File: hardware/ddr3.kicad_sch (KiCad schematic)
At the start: 8 parts, among them U2 H5TQ4G63EFR

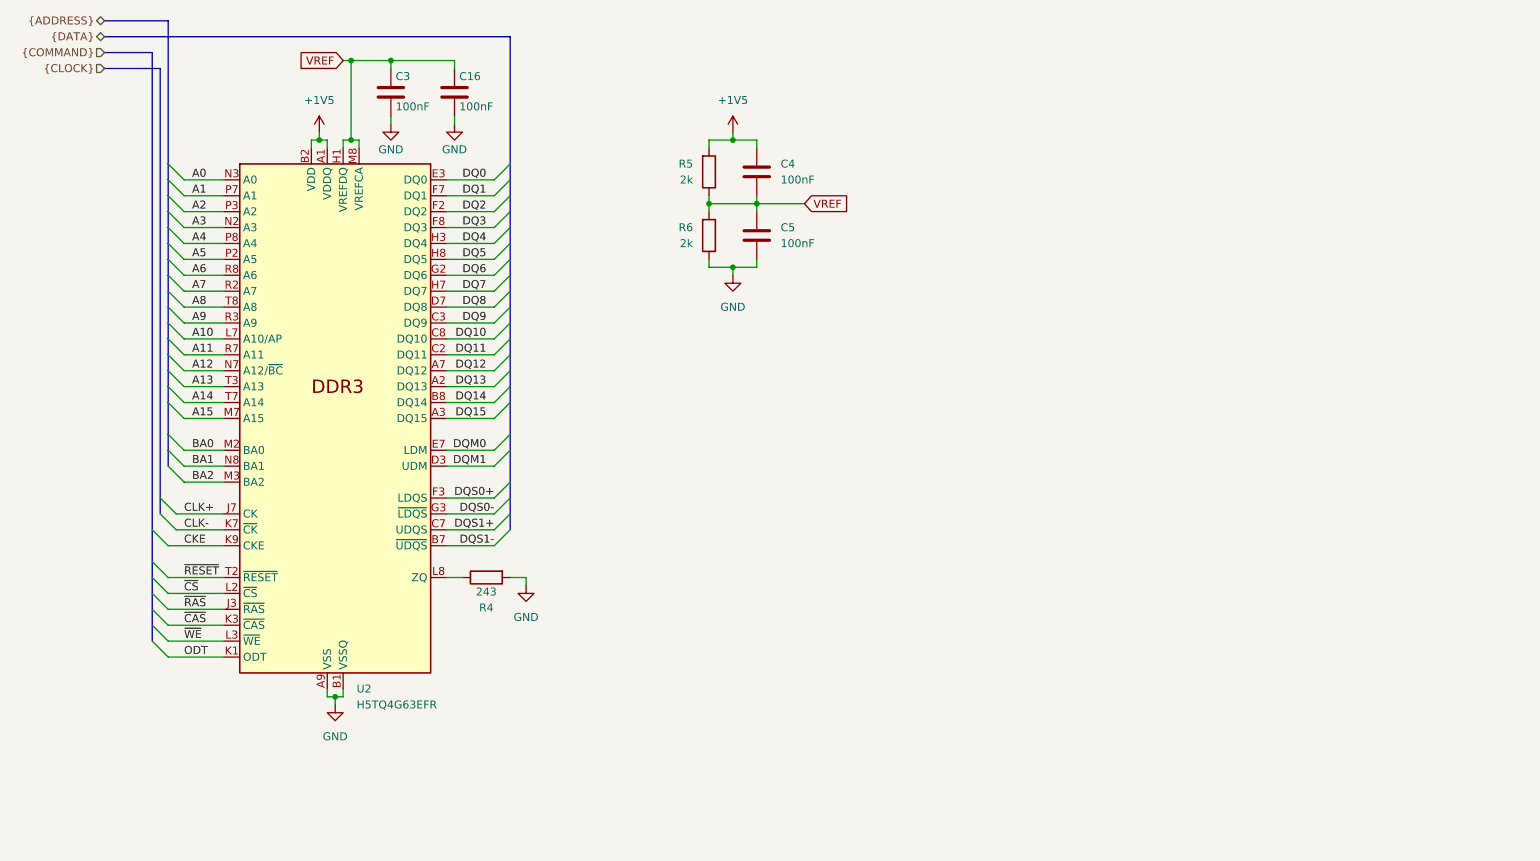
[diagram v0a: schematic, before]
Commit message: Decoupled DDR3 and drew RJ45 connector
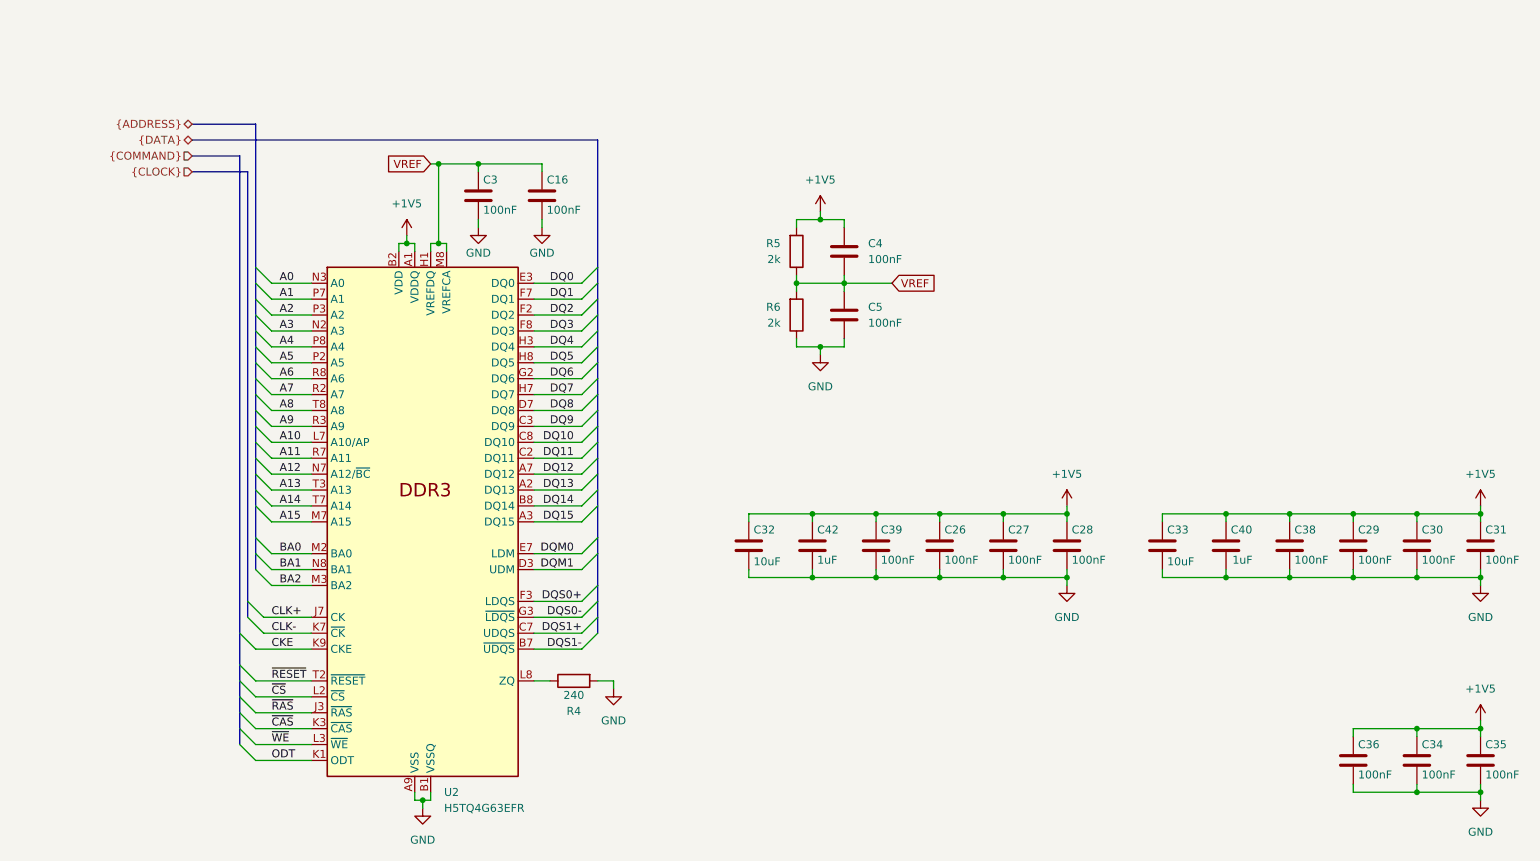
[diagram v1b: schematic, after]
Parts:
- added C26, C27, C28, C29, C30, C31, C34, C35, C36, C38, C39: 100nF, Capacitor_SMD:C_0402_1005Metric, symbol Device:C
- added C32, C33: 10uF, Capacitor_SMD:C_0603_1608Metric, symbol Device:C
- added C40, C42: 1uF, Capacitor_SMD:C_0402_1005Metric, symbol Device:C
- C16, C3, C4, C5: LCSC Part # (none) -> C1525
- R4: value 243 -> 240; LCSC Part # (none) -> C23350
- R5, R6: footprint Resistor_SMD:R_0603_1608Metric -> Resistor_SMD:R_0402_1005Metric; LCSC Part # (none) -> C4109
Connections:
- net +1V5: now also C26.1, C27.1, C28.1, C29.1, C30.1, C31.1, C32.1, C33.1, C34.1, C35.1, C36.1, C38.1, C39.1, C40.2, C42.2
- net GND: now also C26.2, C27.2, C28.2, C29.2, C30.2, C31.2, C32.2, C33.2, C34.2, C35.2, C36.2, C38.2, C39.2, C40.1, C42.1
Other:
- company: (none) -> Icy Electronics
- title: (none) -> Icepi CM0
- moved on the sheet: C16, C3, C4, C5, R4, R5, R6, U2

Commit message: Initial layout
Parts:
- renumbered C5 to C10, C39 to C11, C26 to C12, C27 to C13, C28 to C14, C33 to C15, C40 to C16, C38 to C17, C29 to C18, C36 to C19, C30 to C20, C34 to C21, C31 to C22, C35 to C23, C3 to C5, C16 to C6, C32 to C7, C42 to C8, C4 to C9, R4 to R5, R5 to R6, R6 to R7

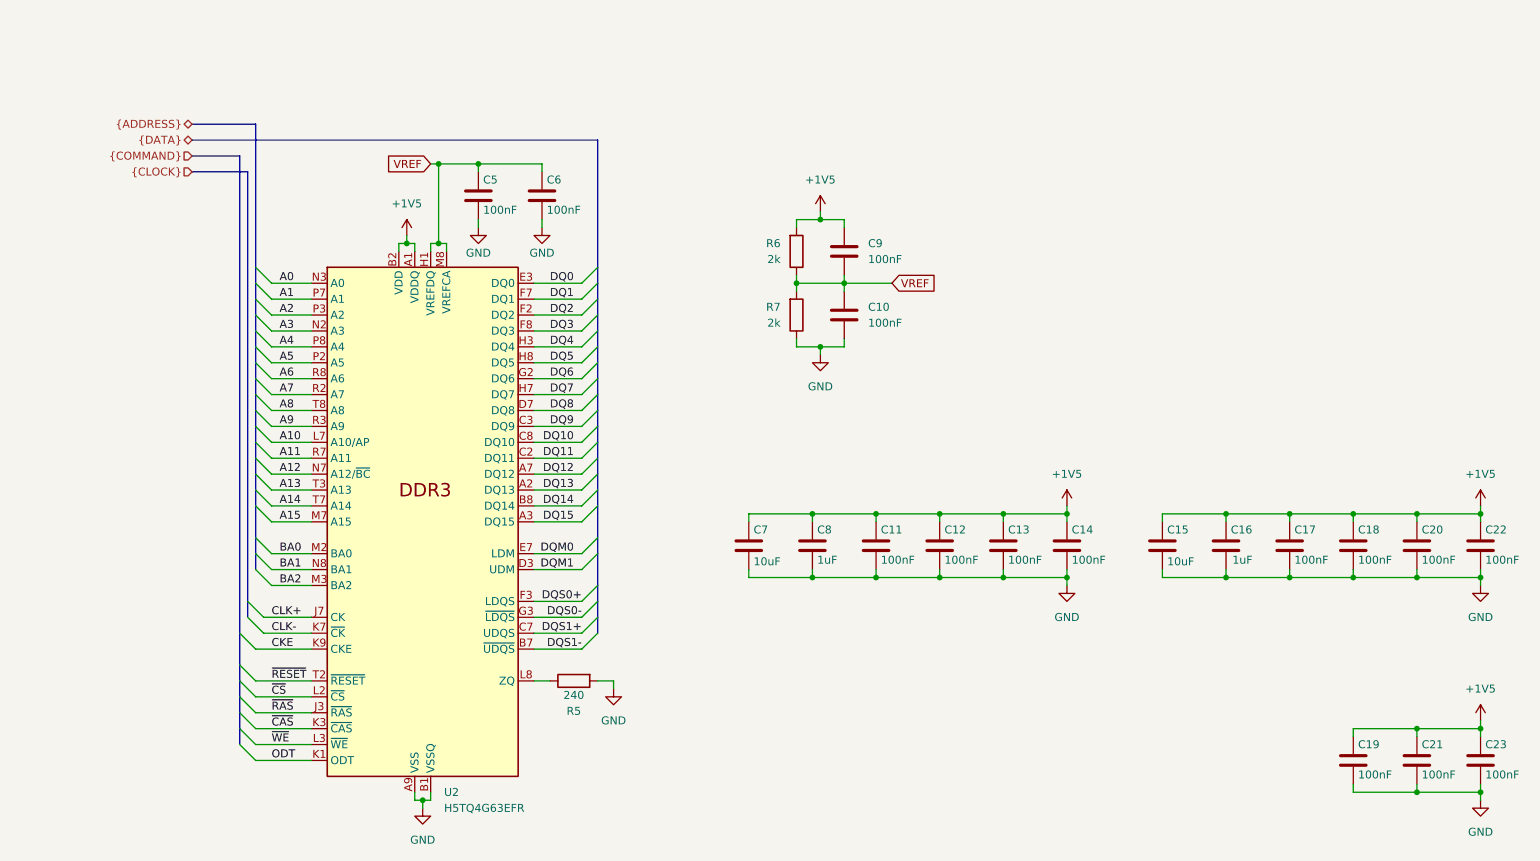
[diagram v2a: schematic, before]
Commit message: Finished DC DC converters and started decoupling the CPU
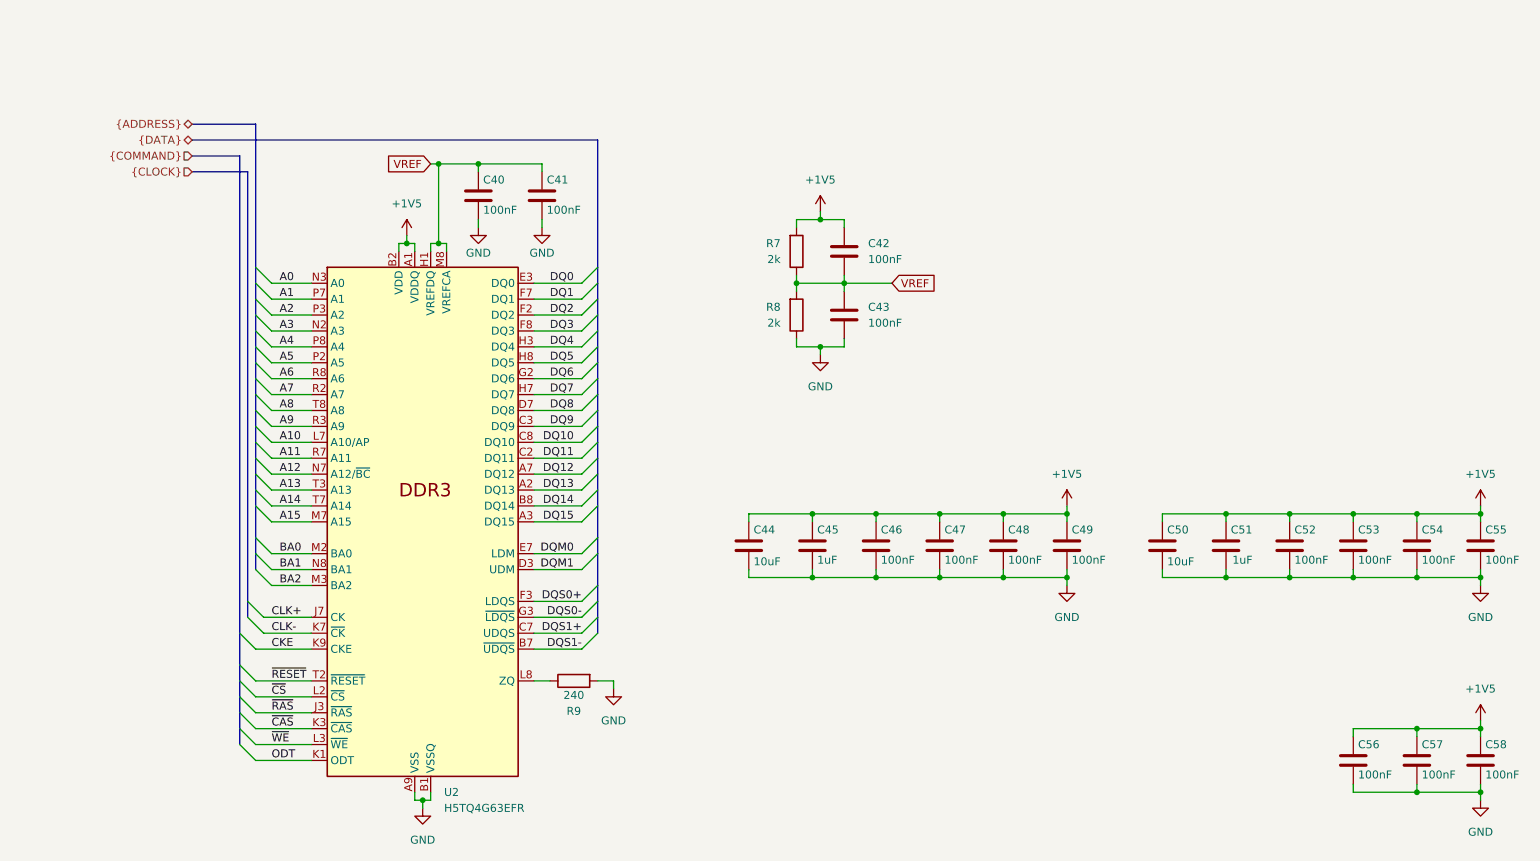
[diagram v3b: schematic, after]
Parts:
- renumbered C5 to C40, C6 to C41, C9 to C42, C10 to C43, C7 to C44, C8 to C45, C11 to C46, C12 to C47, C13 to C48, C14 to C49, C15 to C50, C16 to C51, C17 to C52, C18 to C53, C20 to C54, C22 to C55, C19 to C56, C21 to C57, C23 to C58, R6 to R7, R7 to R8, R5 to R9
